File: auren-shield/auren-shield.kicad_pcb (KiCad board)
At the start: 4 copper layers, 38 x 40 mm, 49 parts, among them J1 Tympan_SJ-3523-SMT-TR, J2 Tympan_SJ-3524-SMT-TR-PI, J3 USB_B_Mini, J4 USB_B_Mini, J5 Conn_01x01, J6 Conn_01x01, P1 CONN_01X06, P2 CONN_01X06, P3 CONN_01X06, P4 CONN_01X06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

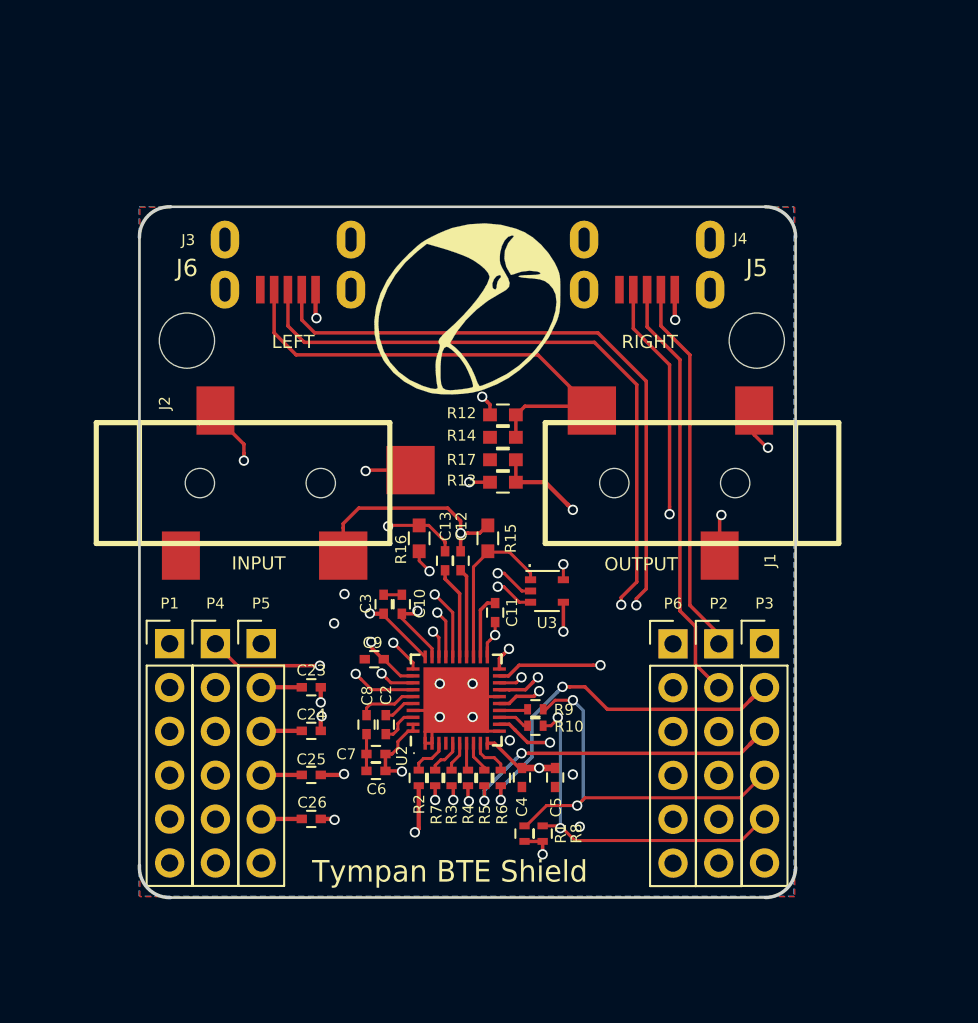
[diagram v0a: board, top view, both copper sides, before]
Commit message: HDMI A connector routing
also moved the Rs and Cs above the AIC closer to it. There is some room to move the HDMI left and down to shorten the board, but also crowd the layout. tradeoffs.
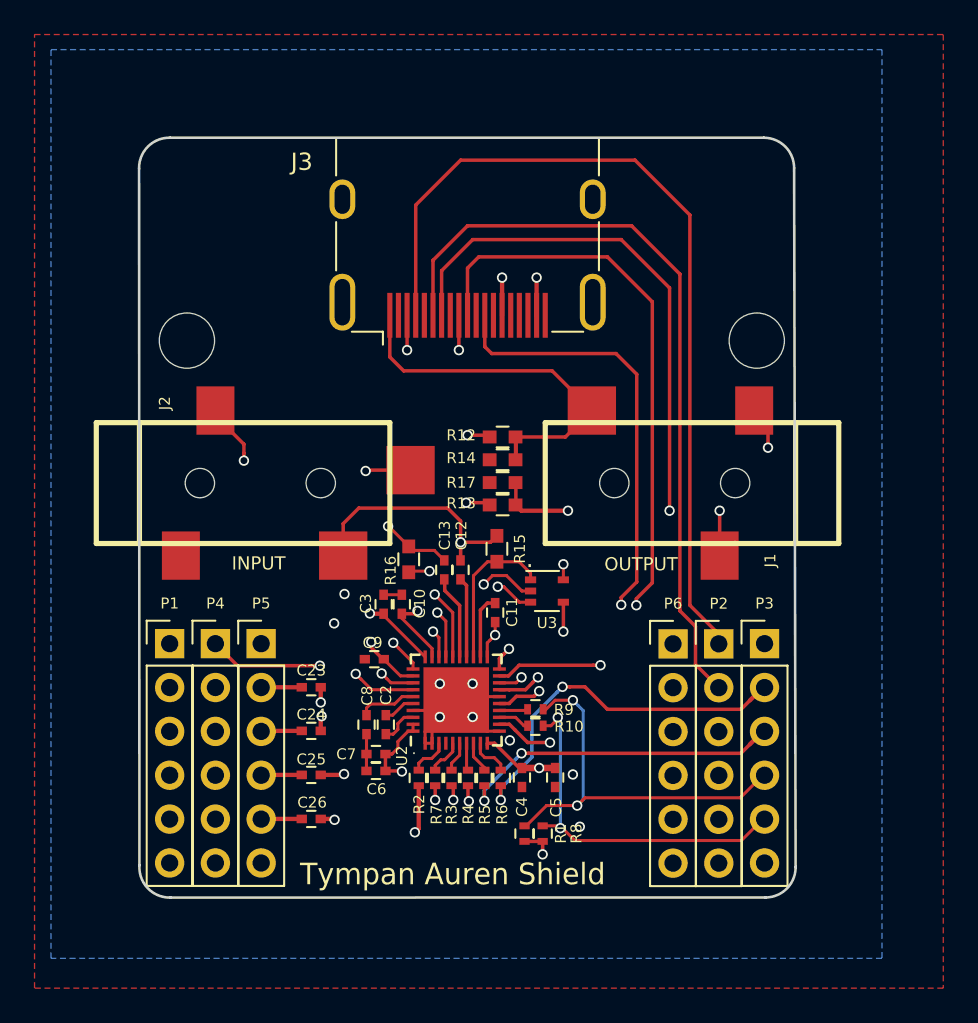
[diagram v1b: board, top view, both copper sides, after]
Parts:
- removed the G*** at (133.8, 52.4)
- removed J4: USB_B_Mini, Tympan:USB_MINI_MOLEX_51387-0578
- J3: value USB_B_Mini -> HDMI A; footprint Tympan:USB_MINI_MOLEX_51387-0578 -> Connector_Video:HDMI_A_Molex_208658-1001_Horizontal
- moved J3 10.6 mm to (133.8, 49.5), turned to 90 degrees
- moved R16 1.36 mm to (130.4, 66.9)
- moved R17 1.32 mm to (135.9, 62.5)
- moved R13 1.32 mm to (135.9, 63.7)
- moved R14 1.30 mm to (135.9, 61.1)
- moved R12 1.28 mm to (135.9, 59.8)
- moved R15 0.80 mm to (135.6, 66.3)
- moved C13 0.53 mm to (132.5, 67.5)
- moved C12 0.53 mm to (133.4, 67.5)
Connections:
- J3 pad 1: +3.3V -> /HPL_1
- J3 pad 2: /PDM_CLK1 -> GND
- J3 pad 3: /PDM_DAT1 -> GND
- J3 pad 4: /HPL_1 -> /PDM_CLK
- J3 pad 6: GND -> /PDM_DAT
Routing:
- net /PDM_CLK: track 21.8 -> 50.1 mm
- net /PDM_DAT: track 24.7 -> 44.3 mm
- net /HPR_1: track 30.0 -> 46.3 mm
- net /PDM_DAT1: track 64.9 -> 53.1 mm
- net /HPL_1: track 28.6 -> 23.3 mm
- net /PDM_CLK1: track 61.4 -> 57.8 mm
- net GND: track 76.1 -> 78.6 mm, vias 8 -> 10
- net Net-(U2-HPL): track 19.6 -> 17.9 mm
- net Net-(J2-T): track 12.8 -> 14.4 mm
- net +3.3V: track 15.4 -> 16.3 mm
- net /MICBIAS: track 9.76 -> 8.99 mm
- net /IN3_L: track 5.16 -> 4.64 mm
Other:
- board size 38 x 40 mm -> 38 x 44 mm
- board text added: "Designed in Troy, NY USA"
- board text added: "TYMPAN AUREN SHIELD"
- board text added: "Tympan Auren Shield"
- board text removed: "Designed in Brooklyn, NY USA"
- board text removed: "LEFT"
- board text removed: "RIGHT"
- board text removed: "TYMPAN EARPIECE SHIELD"
- board text removed: "Tympan BTE Shield"

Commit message: added Rs per #5
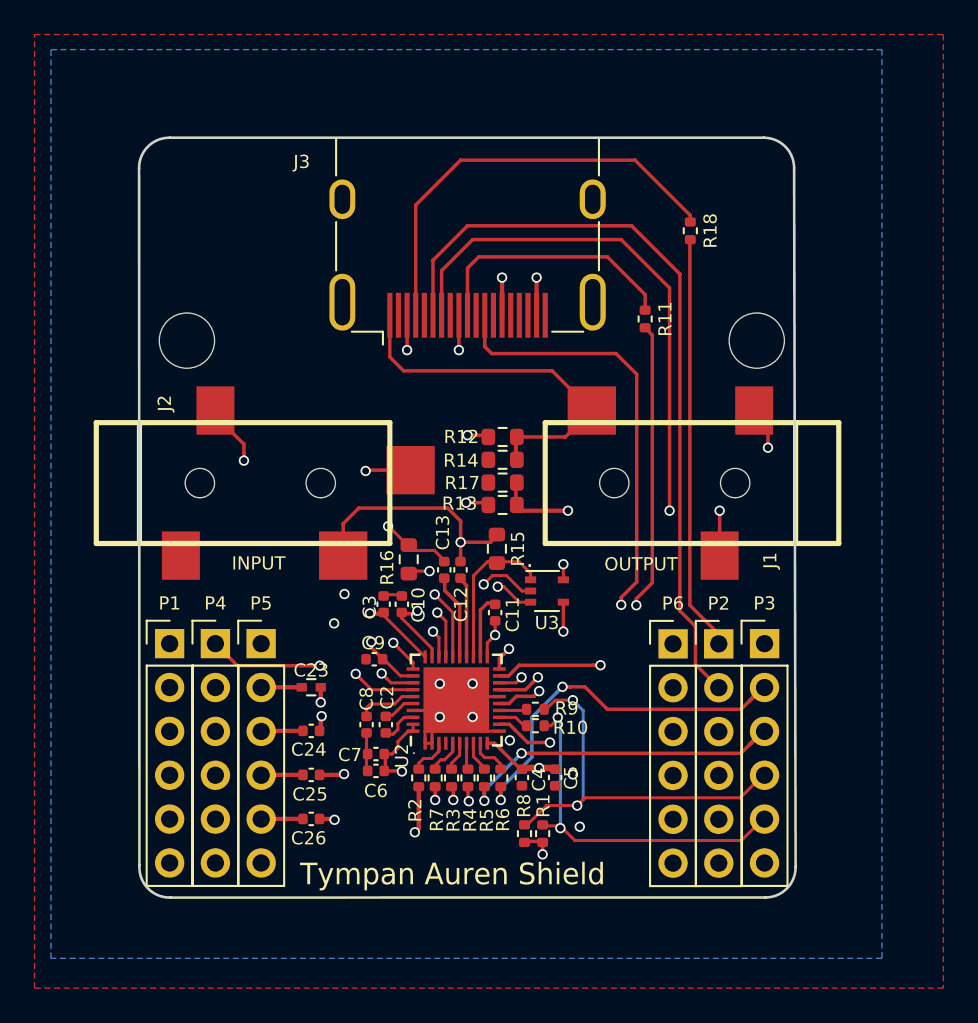
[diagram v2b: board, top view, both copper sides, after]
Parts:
- added R11: 33R, Resistor_SMD:R_0402_1005Metric, F.Cu at (144.1, 53.0)
- added R18: 33R, Resistor_SMD:R_0402_1005Metric, F.Cu at (146.8, 47.9)
- C10, C11, C12, C13, C2, C24, C25, C26, C3, C4, C5, C6, C7, C8, C9: footprint Capacitors_SMD:C_0402 -> Capacitor_SMD:C_0402_1005Metric
- J3: value HDMI A -> HDMI_A_Molex_208658-1001
- R1, R10, R2, R3, R4, R5, R6, R7, R8, R9: footprint Resistors_SMD:R_0402 -> Resistor_SMD:R_0402_1005Metric
- R12, R13, R14, R15, R16, R17: footprint Capacitors_SMD:C_0603 -> Resistor_SMD:R_0603_1608Metric
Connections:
- J3 pad 10: /PDM_CLK1 -> Net-(J3-Pin_10)
- J3 pad 4: /PDM_CLK -> Net-(J3-Pin_4)
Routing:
- net /PDM_CLK: track 50.1 -> 24.0 mm
- net Net-(J3-Pin_4): track 0.00 -> 25.1 mm
- net /PDM_CLK1: track 57.8 -> 41.7 mm
- net Net-(J3-Pin_10): track 0.00 -> 15.1 mm

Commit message: Removed audio jacks. Resized PCB
Cleaned up around GND_SNS circuit
PCB is now 38mm x 40mm (was x 44mm)
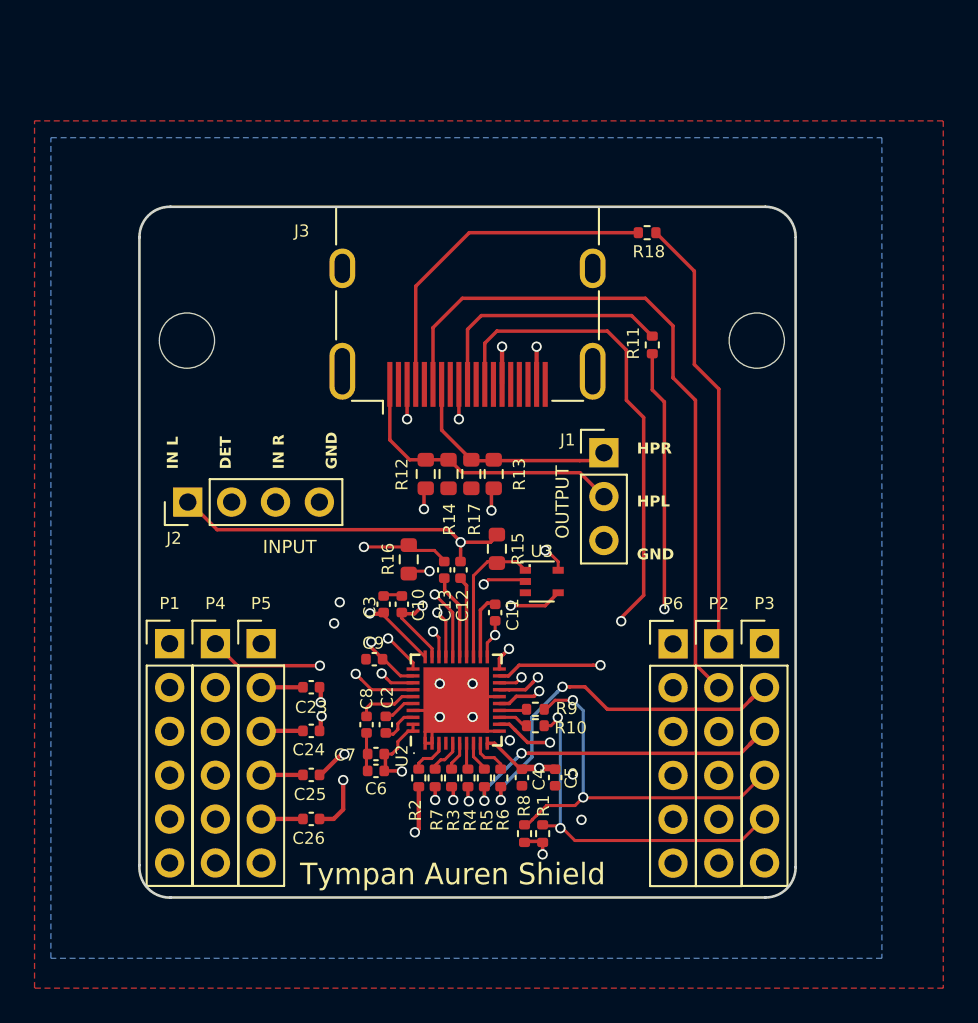
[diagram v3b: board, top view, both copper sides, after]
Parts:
- C23: footprint Capacitors_SMD:C_0402 -> Capacitor_SMD:C_0402_1005Metric
- J1: value Tympan_SJ-3523-SMT-TR -> Headphone Out; footprint Tympan:SJ-3523-SMT-TR -> Connector_PinHeader_2.54mm:PinHeader_1x03_P2.54mm_Vertical
- J2: value Tympan_SJ-3524-SMT-TR-PI -> MIC In; footprint Tympan:SJ-3524-SMT-TR -> Connector_PinHeader_2.54mm:PinHeader_1x04_P2.54mm_Vertical
- moved J1 7.80 mm to (141.7, 60.7), turned to 0 degrees
- moved R12 4.94 mm to (131.4, 62.0), turned to 90 degrees
- moved J3 4.00 mm to (133.8, 53.5)
- moved R14 3.24 mm to (132.8, 62.0), turned to -90 degrees
- moved R18 2.50 mm to (144.2, 48.0), turned to 0 degrees
- moved R17 1.88 mm to (134.1, 62.0), turned to -90 degrees
- moved R13 1.86 mm to (135.4, 62.0), turned to 90 degrees
- moved R11 1.56 mm to (144.6, 54.5)
- moved J2 1.30 mm to (117.7, 63.6), turned to 90 degrees
- moved U3 0.63 mm to (138.2, 68.2)
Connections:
- C12 pad 2: Net-(J2-T) -> Net-(J2-Pin_1)
- J1 pad 1: GND -> /HPR_1
- J1 pad 3: /HPR_1 -> GND
- J2 pad 1: GND -> Net-(J2-Pin_1)
- J2 pad 2: Net-(J2-T) -> /MICDET
- J2 pad 4: /MICDET -> GND
- R15 pad 2: Net-(J2-T) -> Net-(J2-Pin_1)
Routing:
- net /HPR_1: track 46.3 -> 14.0 mm, vias 3 -> 0
- net GND: track 78.6 -> 51.5 mm, vias 10 -> 8
- net Net-(J2-Pin_1): track 0.00 -> 20.7 mm, vias 0 -> 1
- net Net-(J2-T): track 14.4 -> 0.00 mm, vias 1 -> 0
- net Net-(J2-Pin_3): track 17.9 -> 11.2 mm, vias 2 -> 1
- net /HPL_1: track 23.3 -> 17.3 mm
- net Net-(U2-HPL): track 17.9 -> 12.1 mm
- net Net-(J3-Pin_4): track 25.1 -> 19.9 mm
- net /PDM_DAT: track 44.3 -> 40.5 mm
- net /PDM_DAT1: track 53.1 -> 54.6 mm
- net /PDM_CLK: track 24.0 -> 25.2 mm
- net /PDM_CLK1: track 41.7 -> 40.6 mm
- net /M_BIAS_1: track 23.2 -> 22.1 mm
- net /MICBIAS: track 8.99 -> 8.25 mm
- net Net-(U3-O/I): track 7.98 -> 7.25 mm
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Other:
- board size 38 x 44 mm -> 38 x 40 mm
- board text added: "HPR HPL GND"
- board text added: "IN L DET IN R GND"
